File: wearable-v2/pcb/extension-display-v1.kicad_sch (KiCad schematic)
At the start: 28 parts, among them J16 EA_WF030-39S, J17 JST_AUDIO_OUT, J18 DEBUG_HERALD, J19 FTDI_HERALD, J9 HERALD_V2_CONN_PLUG, U10 ATmega328PB-M, U13 TPA6139A2RGTR, U16 DRV2605LDGS, U17 LRA-C08-005.001, U7 MX25R6435FZNIL0, Y2 8Mhz

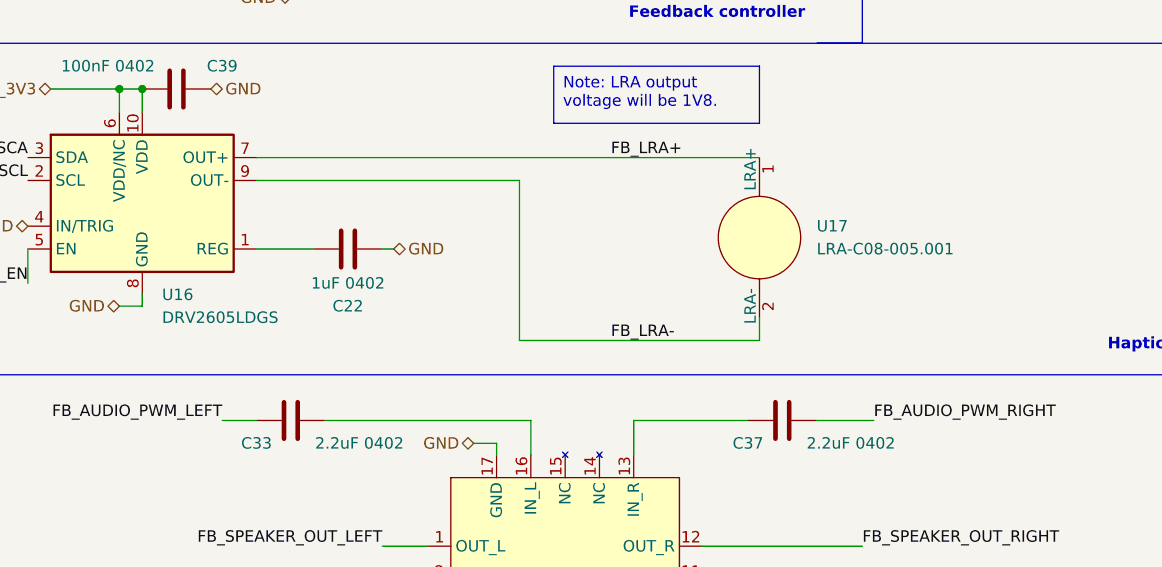
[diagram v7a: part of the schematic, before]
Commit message: Updated LRA, BOM. Added first 3D model
Signed-off-by: Adam Fowler <adam@adamfowler.org>
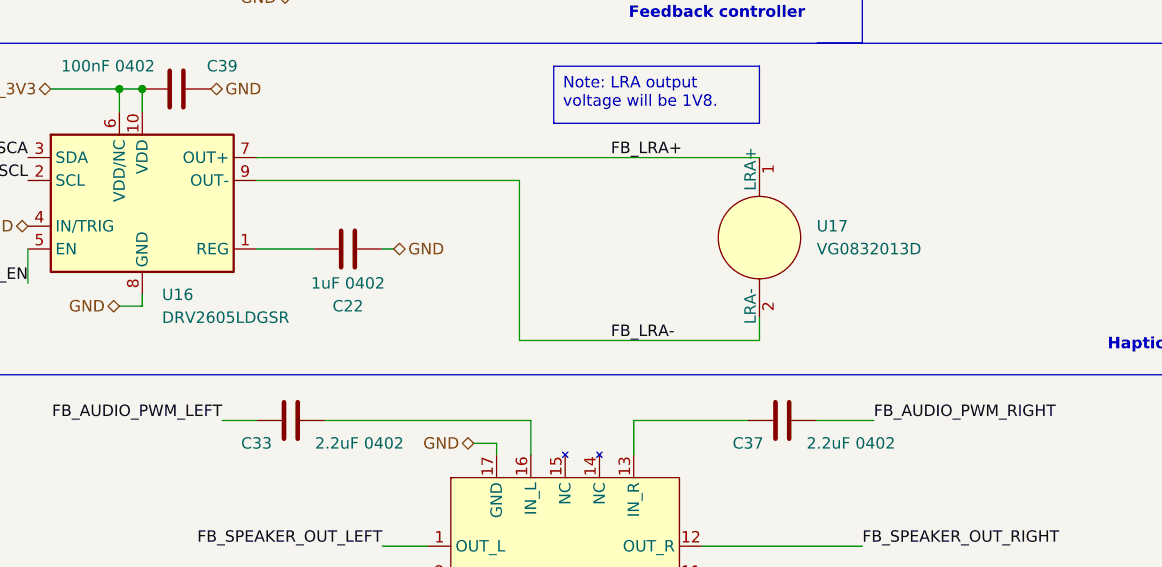
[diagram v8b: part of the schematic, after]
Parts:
- U16: value DRV2605LDGS -> DRV2605LDGSR; MPN DRV2605LDGS -> DRV2605LDGSR
- U17: value LRA-C08-005.001 -> VG0832013D; MPN C08-005.001 -> VG0832013D
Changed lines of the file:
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@@
       (effects (font (size 1.27 1.27)) (justify left))
     )
-    (property "Value" "LRA-C08-005.001" (at 125.73 134.62 0)
+    (property "Value" "VG0832013D" (at 125.73 134.62 0)
       (effects (font (size 1.27 1.27)) (justify left))
     )
@@
       (effects (font (size 1.27 1.27)) hide)
     )
-    (property "Datasheet" "https://catalogue.precisionmicrodrives.com/product/datasheet/c08-005-001-8mm-linear-resonant-actuator-3mm-type-datasheet.pdf" (at 119.38 147.32 0)
-      (effects (font (size 1.27 1.27)) hide)
-    )
-    (property "MPN" "C08-005.001" (at 119.38 133.35 0)
-      (effects (font (size 1.27 1.27)) hide)
-    )
-    (property "Description" "LRA, 1V8, 8mm diameter, 3mm height" (at 119.38 133.35 0)
+    (property "Datasheet" "https://www.vybronics.com/coin-vibration-motors/lra/v-g0832013d" (at 119.38 147.32 0)
+      (effects (font (size 1.27 1.27)) hide)
+    )
+    (property "MPN" "VG0832013D" (at 119.38 133.35 0)
+      (effects (font (size 1.27 1.27)) hide)
+    )
+    (property "Description" "AC Motor Vibration, LRA 1.8VAC" (at 119.38 133.35 0)
       (effects (font (size 1.27 1.27)) hide)
     )
@@
       (effects (font (size 1.27 1.27)) (justify left))
     )
-    (property "Value" "DRV2605LDGS" (at 52.9941 142.24 0)
+    (property "Value" "DRV2605LDGSR" (at 52.9941 142.24 0)
       (effects (font (size 1.27 1.27)) (justify left))
     )
@@
       (effects (font (size 1.27 1.27)) hide)
     )
-    (property "MPN" "DRV2605LDGS" (at 50.8 129.54 0)
-      (effects (font (size 1.27 1.27)) hide)
-    )
+    (property "MPN" "DRV2605LDGSR" (at 50.8 129.54 0)
+      (effects (font (size 1.27 1.27)) hide)
+    )
